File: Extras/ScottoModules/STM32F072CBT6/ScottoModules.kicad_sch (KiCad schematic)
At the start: 30 parts, among them J1 USB_C, SW1 SW_Push, U1 STM32F072CBT6, U3 XC6206, U4 USBLC6-2SC6

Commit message: Add Template
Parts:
- removed D1, D2, D3, D4, D5, D6: Diode, ScottoKeebs_Components:Diode_SOD-123, symbol ScottoKeebs:Placeholder_Diode
- removed S1, S2, S3, S4, S5, S6: Keyswitch, ScottoKeebs_Scotto:MX_1.00u, symbol ScottoKeebs:Placeholder_Keyswitch
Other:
- note removed: "Matrix"
- moved on the sheet: C1, C2, C3, C4, C5, C6, C7, C8, C9, F1, J1, R1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

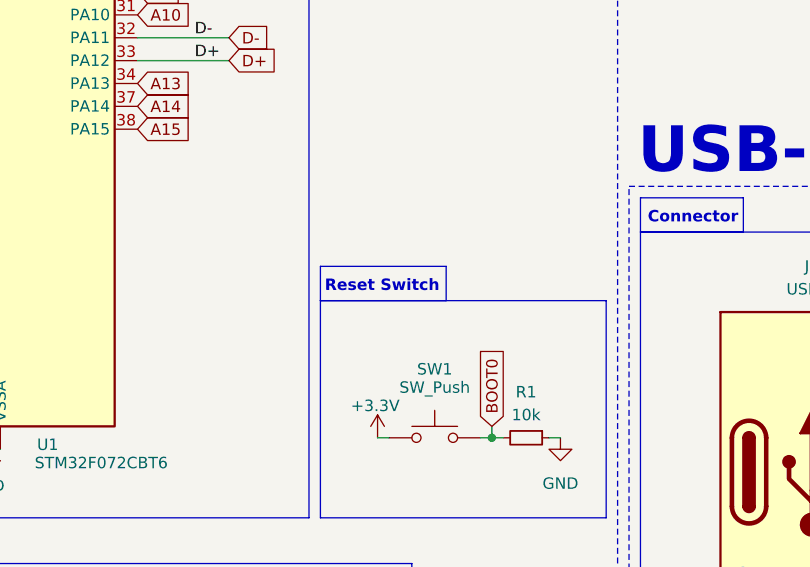
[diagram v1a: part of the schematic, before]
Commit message: Rename reset to boot button for clarity
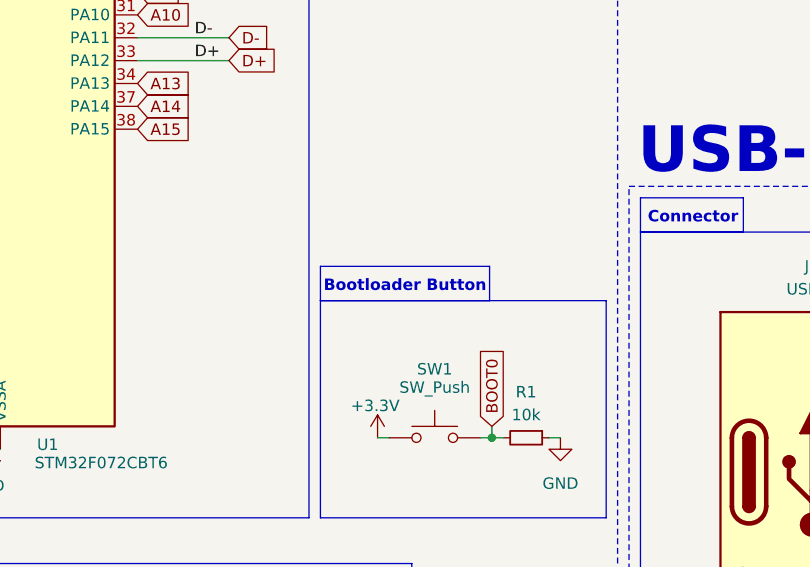
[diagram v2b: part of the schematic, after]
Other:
- note added: "Bootloader Button"
- note removed: "Reset Switch"
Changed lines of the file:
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@@
 	(rectangle
 		(start 85.09 224.79)
-		(end 99.06 228.6)
+		(end 103.886 228.6)
 		(stroke
 			(width 0)
@@
 		)
 	)
-	(text "Reset Switch"
+	(text "Bootloader Button"
 		(exclude_from_sim no)
-		(at 91.948 227.076 0)
+		(at 94.488 227.076 0)
 		(effects
 			(font
